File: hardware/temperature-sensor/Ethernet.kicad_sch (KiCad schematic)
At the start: 27 parts, among them IC2 PM8803TR, J1 1149611, T1 PT61018PEL, U2 LAN8720A

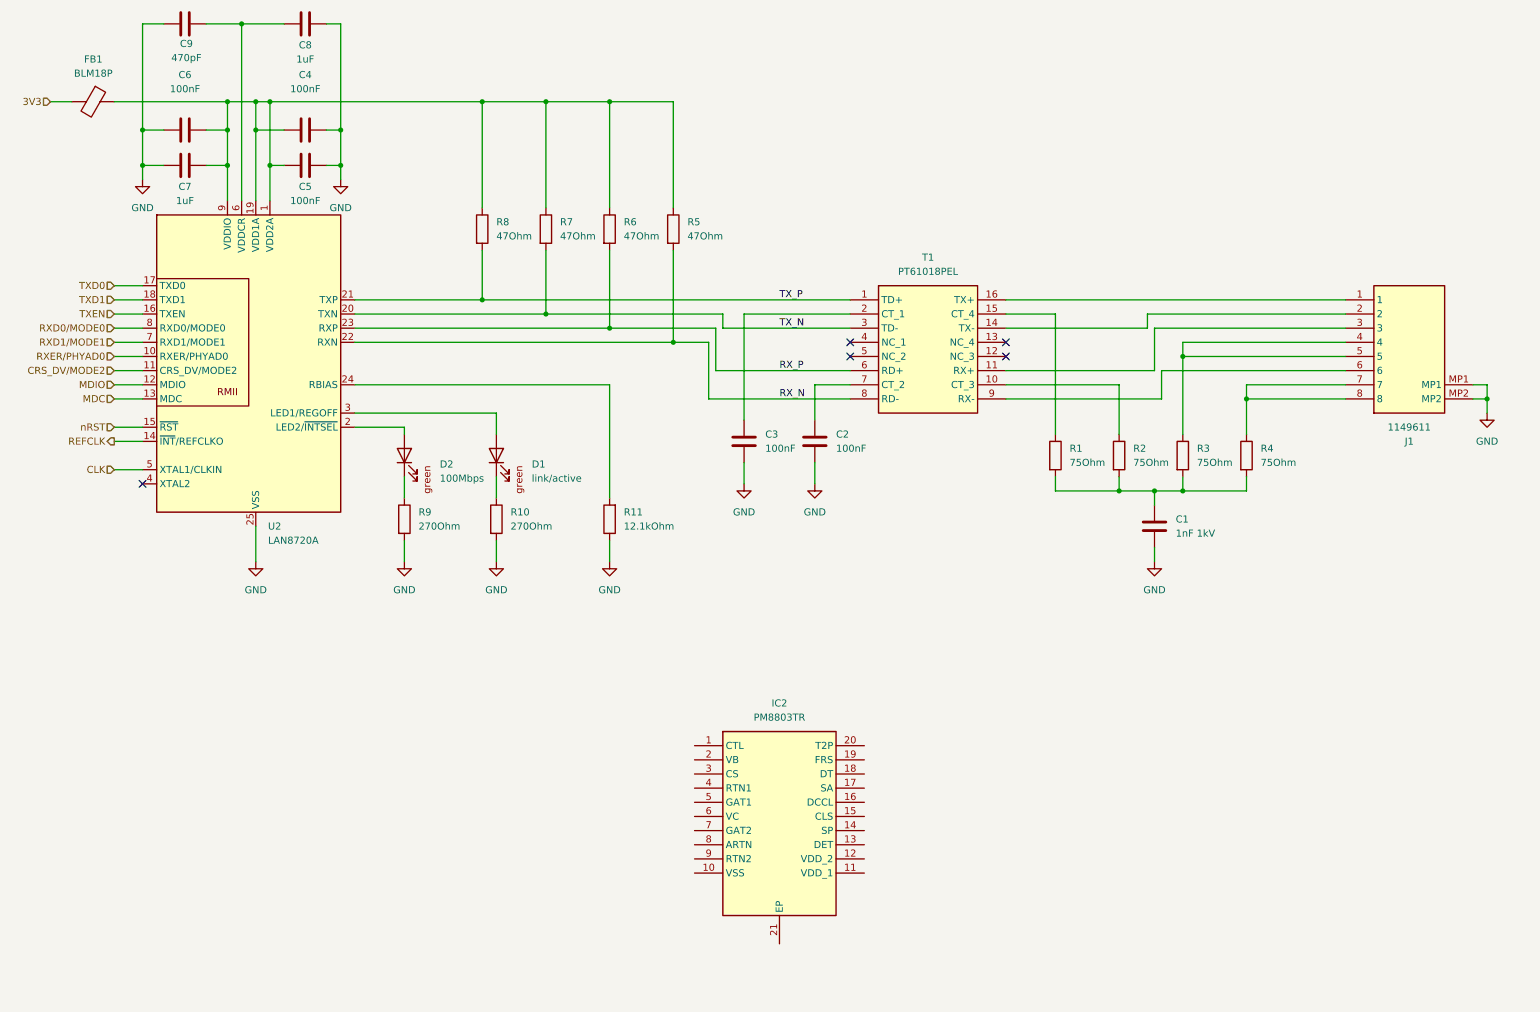
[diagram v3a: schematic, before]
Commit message: replace ethernet transformer
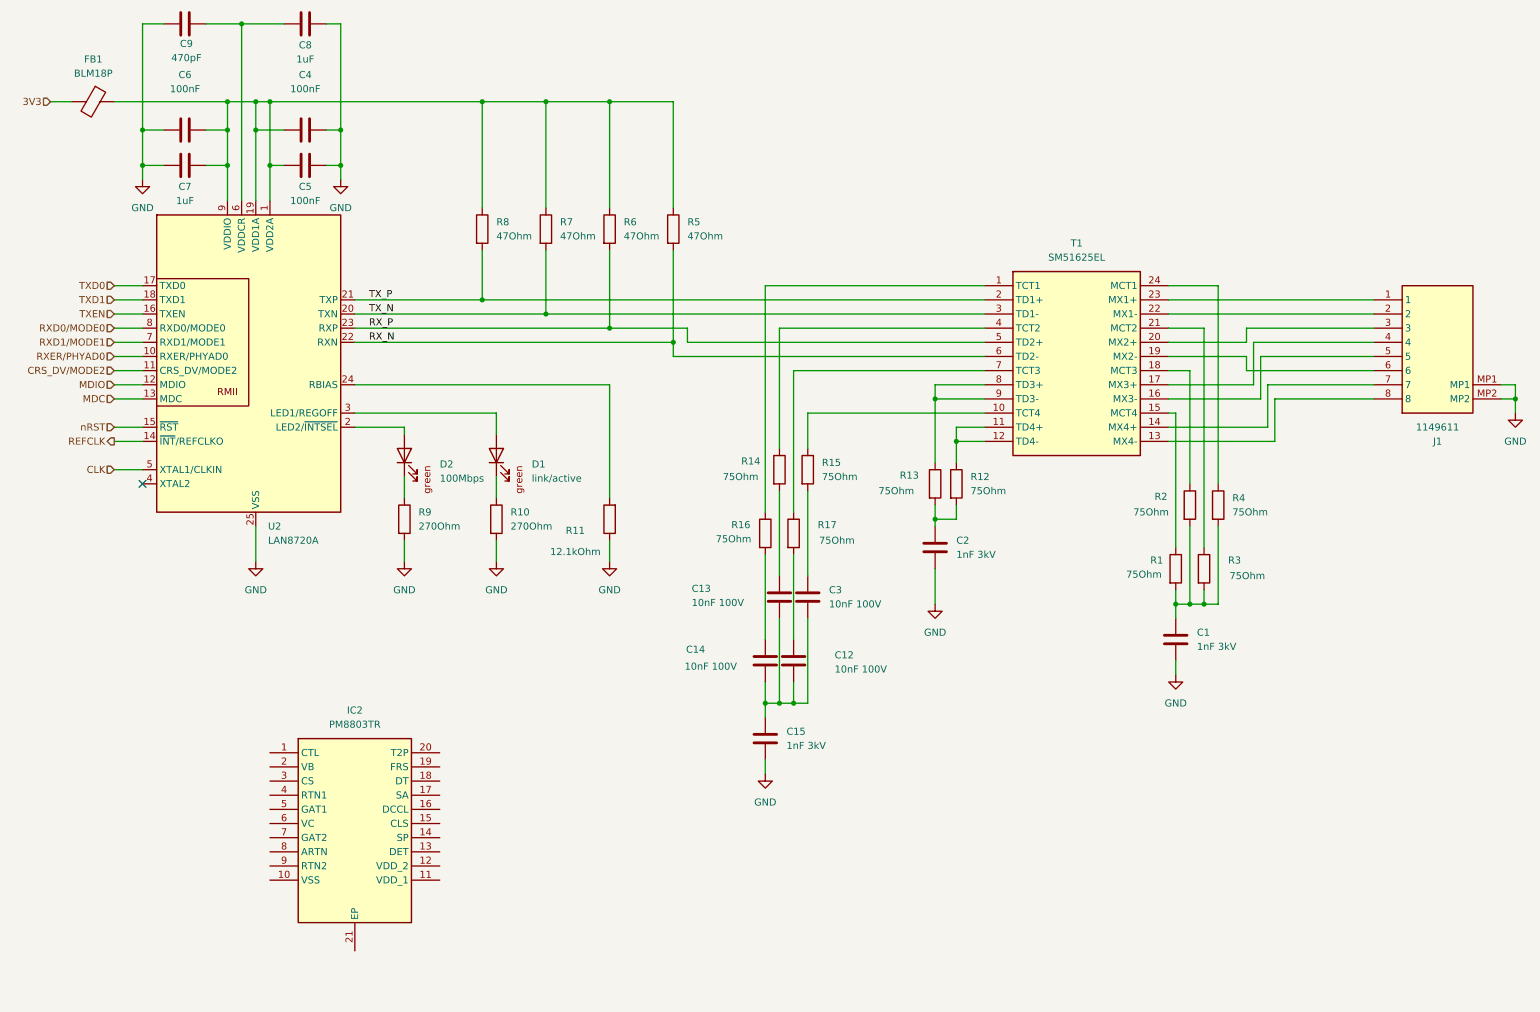
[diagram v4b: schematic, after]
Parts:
- removed C1: 1nF 1kV, benediktibk:C_0603_1608Metric_Pad1.08x0.95mm_HandSolder, symbol benediktibk:C_1nF_SMD_0603_1000V_10%
- removed C2, C3: 100nF, benediktibk:C_0603_1608Metric_Pad1.08x0.95mm_HandSolder, symbol benediktibk:C_100nF_SMD_0603_50V
- removed T1: PT61018PEL, benediktibk:SOIC127P930X565-16N, symbol benediktibk:PT61018PEL
- added C1, C15, C2: 1nF 3kV, benediktibk:C_0603_1608Metric_Pad1.08x0.95mm_HandSolder, symbol benediktibk:C_1nF_SMD_1812_3kV_10%
- added C12, C13, C14, C3: 10nF 100V, benediktibk:C_0603_1608Metric_Pad1.08x0.95mm_HandSolder, symbol benediktibk:C_10nF_SMD_0603_100V_10%
- added R12, R13, R14, R15, R16, R17: 75Ohm, benediktibk:R_0603_1608Metric_Pad0.98x0.95mm_HandSolder, symbol benediktibk:R_75Ohm_SMD_0603_100mW_1%
- added T1: SM51625EL, benediktibk:SOIC127P1600X625-24N, symbol benediktibk:SM51625EL
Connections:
- net GND: now also C1.2, C15.2, C2.2
- net RX_N: now also T1.6 (TD2-)
- net RX_P: now also T1.5 (TD2+)
- net TX_N: now also T1.3 (TD1-)
- net TX_P: now also T1.2 (TD1+)
- net at R1.2, R2.2, R3.2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: now also C1.1
- net at R2.1: now also T1.18 (MCT3)
- net at J1.3: now also T1.20 (MX2+)
- net at J1.2: now also T1.22 (MX1-)
- net at R1.1: now also T1.15 (MCT4)
- net at J1.1: now also T1.23 (MX1+)
- net at J1.6: now also T1.19 (MX2-)
- new net: C14.1, R16.2
- new net: C12.2, C13.2, C14.2, C15.1, C3.2
- new net: C2.1, R12.2, R13.2
- new net: R4.1, T1.24 (MCT1)
- new net: R17.1, T1.7 (TCT3)
- new net: C12.1, R17.2
- new net: R16.1, T1.1 (TCT1)
- new net: C3.1, R15.2
- new net: R13.1, T1.8 (TD3+), T1.9 (TD3-)
- new net: R3.1, T1.21 (MCT2)
- new net: R15.1, T1.10 (TCT4)
- new net: R12.1, T1.11 (TD4+), T1.12 (TD4-)
- new net: J1.8, T1.13 (MX4-)
- new net: J1.7, T1.14 (MX4+)
- new net: J1.5, T1.16 (MX3-)
- new net: J1.4, T1.17 (MX3+)
- new net: R14.1, T1.4 (TCT2)
- new net: C13.1, R14.2
- no-connect marks 5 -> 1
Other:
- moved on the sheet: IC2, J1, R1, R2, R3, R4

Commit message: add bridge rectifier to PoE
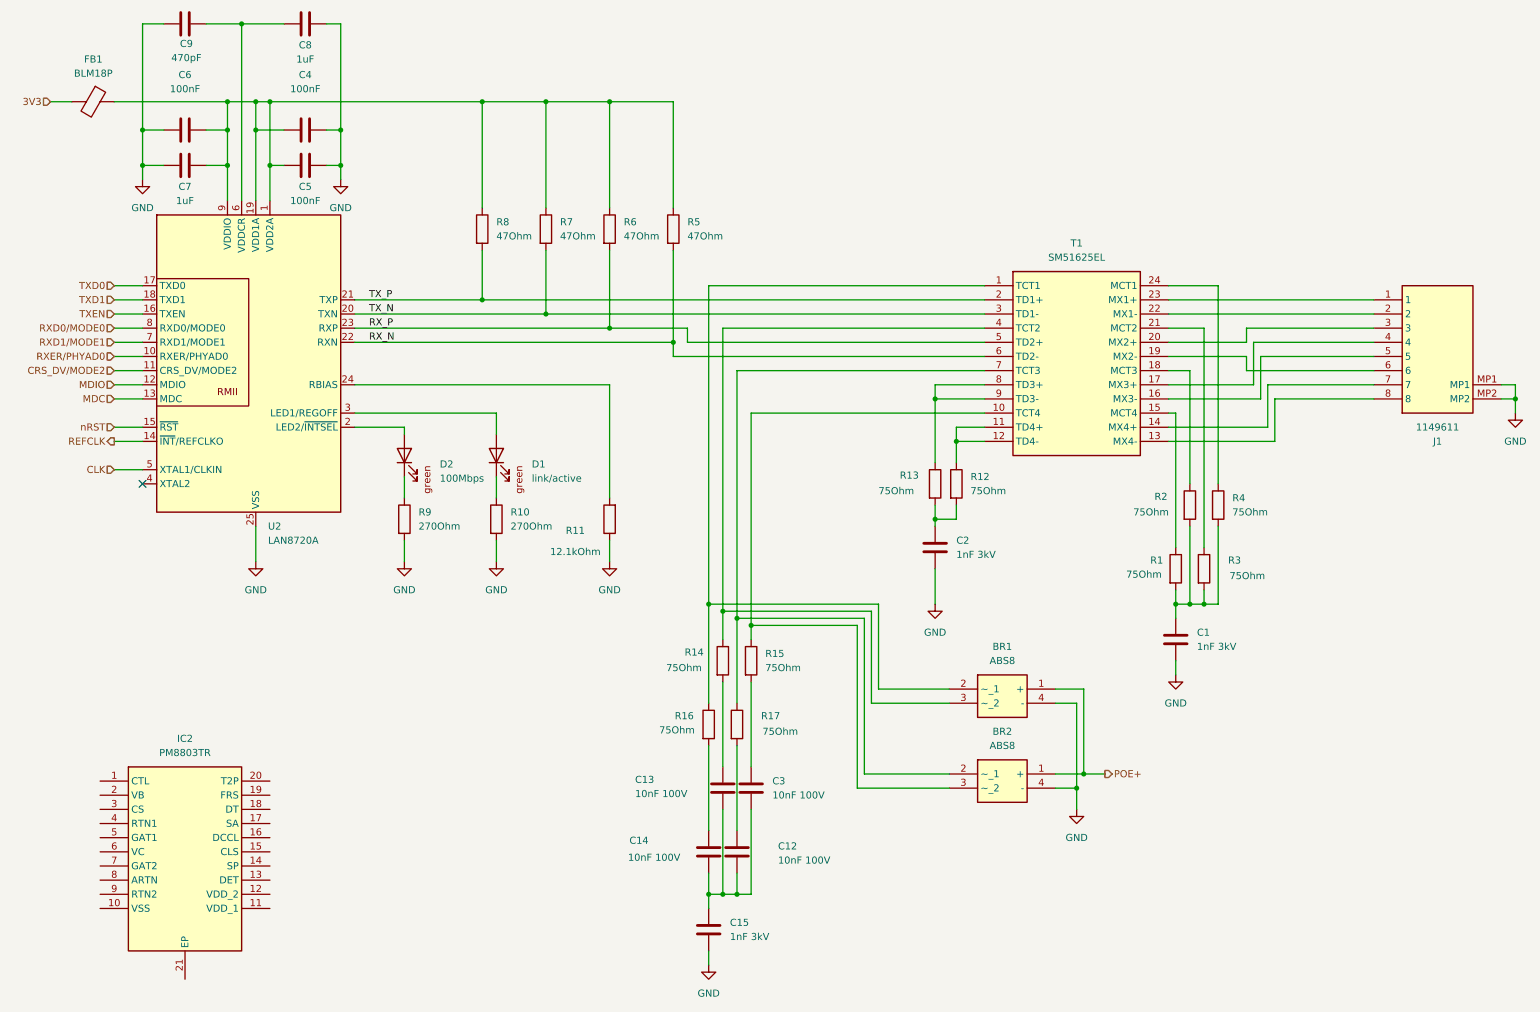
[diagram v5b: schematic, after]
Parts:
- added BR1, BR2: ABS8, benediktibk:ABS8, symbol benediktibk:ABS8
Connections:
- net GND: now also BR1.4 (-), BR2.4 (-)
- net at R17.1, T1.7 (TCT3): now also BR2.2 (~_1)
- net at R16.1, T1.1 (TCT1): now also BR1.2 (~_1)
- net at R15.1, T1.10 (TCT4): now also BR2.3 (~_2)
- net at R14.1, T1.4 (TCT2): now also BR1.3 (~_2)
- new net POE+: BR1.1 (+), BR2.1 (+)
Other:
- moved on the sheet: C12, C13, C14, C15, C3, IC2, R14, R15, R16, R17

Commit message: replace lan transformer with a 2 channel version
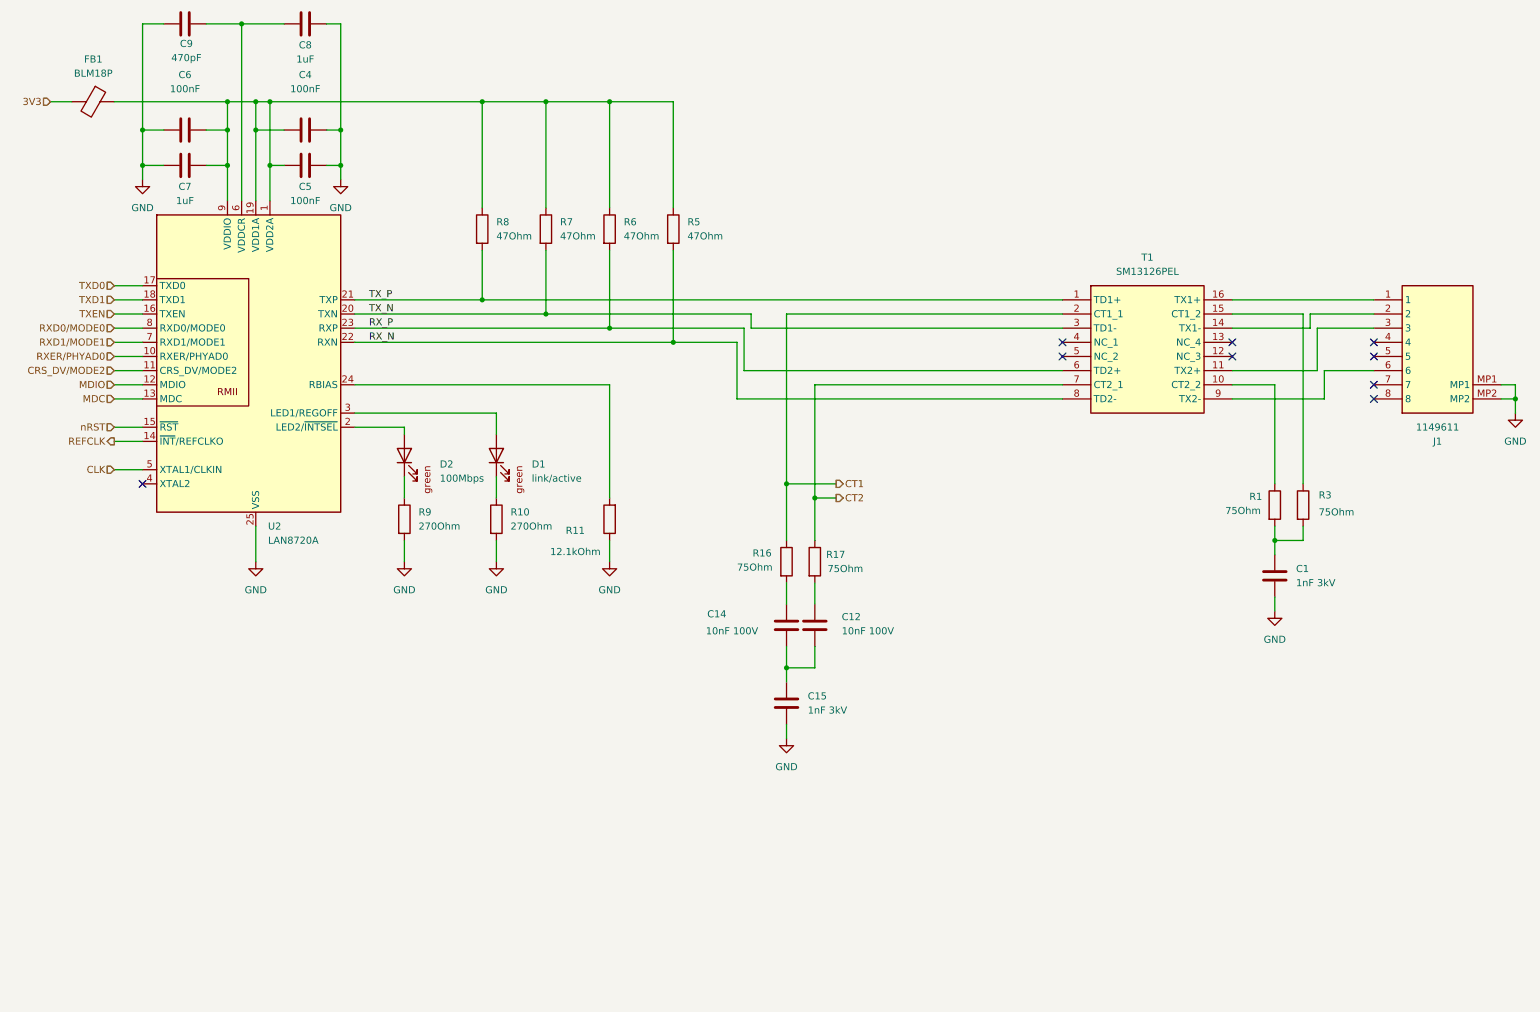
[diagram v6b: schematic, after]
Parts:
- removed BR1, BR2: ABS8, benediktibk:ABS8, symbol benediktibk:ABS8
- removed C13, C3: 10nF 100V, benediktibk:C_0603_1608Metric_Pad1.08x0.95mm_HandSolder, symbol benediktibk:C_10nF_SMD_0603_100V_10%
- removed C2: 1nF 3kV, benediktibk:C_0603_1608Metric_Pad1.08x0.95mm_HandSolder, symbol benediktibk:C_1nF_SMD_1812_3kV_10%
- removed IC2: PM8803TR, benediktibk:SOP65P640X120-21N, symbol benediktibk:PM8803TR
- removed R12, R13, R14, R15, R2, R4: 75Ohm, benediktibk:R_0603_1608Metric_Pad0.98x0.95mm_HandSolder, symbol benediktibk:R_75Ohm_SMD_0603_100mW_1%
- removed T1: SM51625EL, benediktibk:SOIC127P1600X625-24N, symbol benediktibk:SM51625EL
- added T1: SM13126PEL, benediktibk:SM13126PEL, symbol benediktibk:SM13126PEL
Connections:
- net RX_N: now also T1.8 (TD2-)
- net RX_P: now also T1.6 (TD2+)
- net TX_N: now also T1.3 (TD1-)
- net TX_P: now also T1.1 (TD1+)
- net CT1: now reaches R16.1
- net CT1: now also T1.2 (CT1_1)
- net CT2: now reaches R17.1
- net CT2: now also T1.7 (CT2_1)
- net at R3.1: now also T1.15 (CT1_2)
- net at R1.1: now also T1.10 (CT2_2)
- net at J1.6: now also T1.9 (TX2-)
- net at J1.3: now also T1.11 (TX2+)
- net at J1.2: now also T1.14 (TX1-)
- net at J1.1: now also T1.16 (TX1+)
- no-connect marks 1 -> 9
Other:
- moved on the sheet: C1, C12, C14, C15, R1, R16, R17, R3

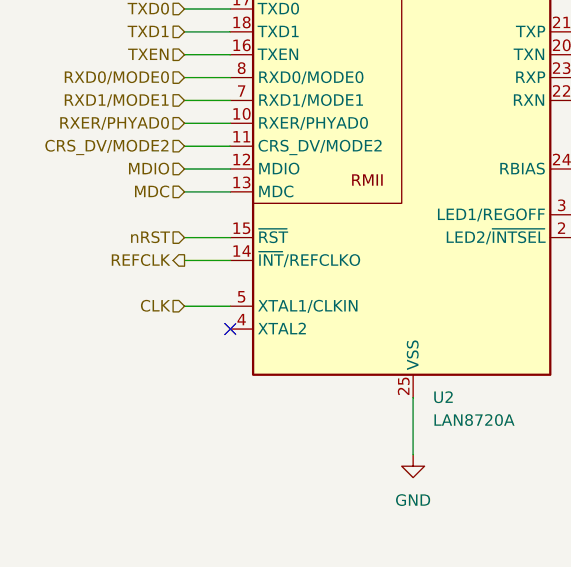
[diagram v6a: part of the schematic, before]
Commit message: work on temperature sensor
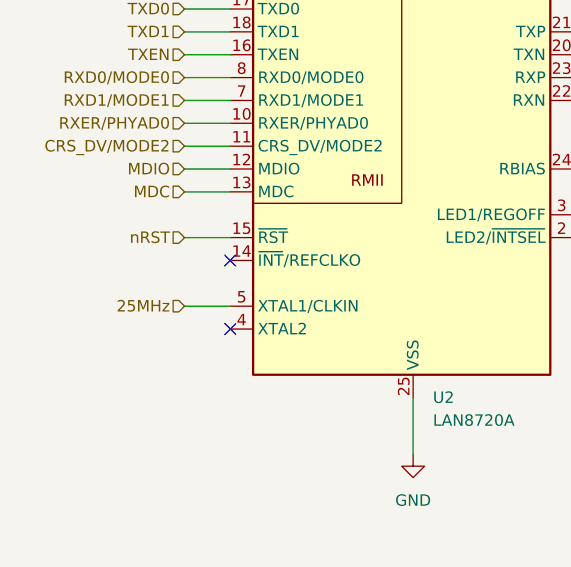
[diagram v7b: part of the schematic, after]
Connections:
- net CLK renamed 25MHz
- net REFCLK: no longer names the net of U2.14 (~{INT}/REFCLKO)
- no-connect marks 9 -> 10
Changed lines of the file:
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@@
+	)
+	(no_connect
+		(at 34.29 90.17)
 	)
 	(no_connect
@@
 		(pts
 			(xy 57.15 40.64) (xy 59.69 40.64)
-		)
-		(stroke
-			(width 0)
-			(type default)
-		)
-	)
-	(wire
-		(pts
-			(xy 29.21 90.17) (xy 34.29 90.17)
 		)
 		(stroke
@@
 		)
 	)
-	(hierarchical_label "CLK"
+	(hierarchical_label "25MHz"
 		(shape input)
 		(at 29.21 95.25 180)
@@
 		(effects
 			(font
-				(size 1.27 1.27)
-			)
-			(justify right)
-		)
-	)
-	(hierarchical_label "REFCLK"
-		(shape output)
-		(at 29.21 90.17 180)
-		(effects
-			(font

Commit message: work on temperature sensor
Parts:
- U2: footprint benediktibk:QFN-24-1EP_4x4mm_P0.5mm_EP2.5x2.5mm -> benediktibk:LAN8720A-CP-ABC; Mouser Part Number (none) -> 579-LAN8720ACPABC
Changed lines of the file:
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@@
 			)
 		)
-		(property "Footprint" "benediktibk:QFN-24-1EP_4x4mm_P0.5mm_EP2.5x2.5mm"
+		(property "Footprint" "benediktibk:LAN8720A-CP-ABC"
 			(at 55.88 104.14 0)
 			(effects
@@
 			(at 54.61 77.47 0)
 			(effects
+				(font
+					(size 1.27 1.27)
+				)
+				(hide yes)
+			)
+		)
+		(property "Mouser Part Number" "579-LAN8720ACPABC"
+			(at 54.61 77.47 0)
+			(effects
